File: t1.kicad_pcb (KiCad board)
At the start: 4 copper layers, 63 x 35.6 mm, 47 parts, among them J1 Barrel_Jack_Switch, J2 USB_B, J3 P1, J4 2x2M, J5 ICSP1, J6 P2, U1 ATmega8U2-AU, Y1 16MHz

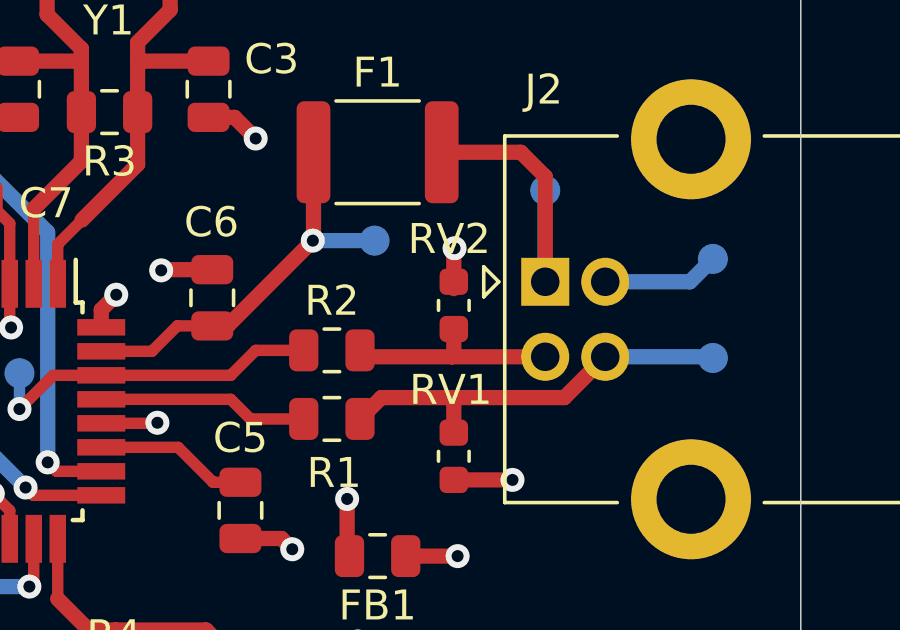
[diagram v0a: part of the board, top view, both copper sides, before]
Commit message: Also renamed varistors in the PCB
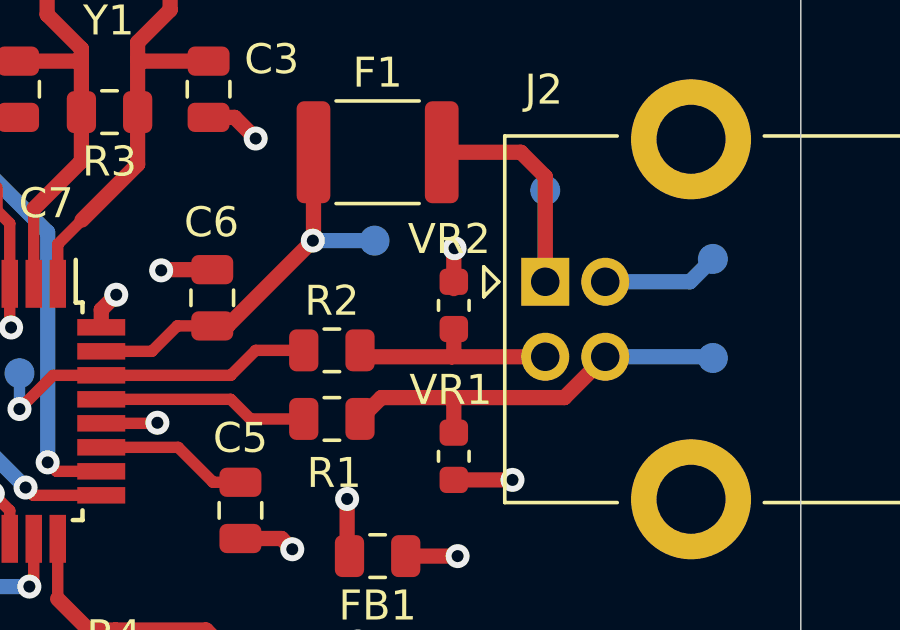
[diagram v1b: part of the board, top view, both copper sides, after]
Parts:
- renumbered RV1 to VR1, RV2 to VR2
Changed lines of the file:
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@@
     (tags "resistor")
     (attr smd)
-    (fp_text reference "RV1" (at -2.2097 0.1016 180) (layer "F.SilkS")
+    (fp_text reference "VR1" (at -2.2097 0.1016 180) (layer "F.SilkS")
       (effects (font (size 1 1) (thickness 0.15)))
     )
@@
     (tags "resistor")
     (attr smd)
-    (fp_text reference "RV2" (at 2.2098 -0.1524 180) (layer "F.SilkS")
-      (effects (font (size 1 1) (thickness 0.15)))
-    )
+    (fp_text reference "VR2" (at 2.2098 -0.1524 180) (layer "F.SilkS")
+      (effects (font (size 1 1) (thickness 0.15)))
+    )
